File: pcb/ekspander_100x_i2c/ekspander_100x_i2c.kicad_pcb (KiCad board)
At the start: 4 copper layers, 500 x 100 mm, 156 parts, among them IC1 ESP32-S3-WROOM-1U-N16R8, J1 DG127A-5.08-06P-14-00AH, J10 DG127A-5.08-06P-14-00AH, J11 DG127A-5.08-06P-14-00AH, J12 DG127A-5.08-06P-14-00AH, J13 DG127A-5.08-06P-14-00AH, J14 DG127A-5.08-06P-14-00AH, J15 DG127A-5.08-06P-14-00AH, J16 DG127A-5.08-06P-14-00AH, J17 DG127A-5.08-06P-14-00AH, J18 DG127A-5.08-06P-14-00AH, J19 DG127A-5.08-06P-14-00AH, J2 DG127A-5.08-06P-14-00AH, J20 DG127A-5.08-06P-14-00AH, J21 DG127A-5.08-06P-14-00AH, J22 DG127A-5.08-06P-14-00AH, J23 DG127A-5.08-06P-14-00AH, J3 DG127A-5.08-06P-14-00AH, J4 DG127A-5.08-06P-14-00AH, J5 DG127A-5.08-06P-14-00AH, J6 DG127A-5.08-06P-14-00AH, J7 DG127A-5.08-06P-14-00AH, J8 DG127A-5.08-06P-14-00AH, J9 DG127A-5.08-06P-14-00AH, K1 G5Q-1A, K10 G5Q-1A, K11 G5Q-1A, K12 G5Q-1A, K13 G5Q-1A, K14 G5Q-1A, K15 G5Q-1A, K16 G5Q-1A, K17 G5Q-1A, K18 G5Q-1A, K19 G5Q-1A, K2 G5Q-1A, K20 G5Q-1A, K21 G5Q-1A, K22 G5Q-1A, K23 G5Q-1A, K24 G5Q-1A, K25 G5Q-1A, K26 G5Q-1A, K27 G5Q-1A, K28 G5Q-1A, K29 G5Q-1A, K3 G5Q-1A, K30 G5Q-1A, K31 G5Q-1A, K32 G5Q-1A, K33 G5Q-1A, K34 G5Q-1A, K35 G5Q-1A, K36 G5Q-1A, K37 G5Q-1A, K38 G5Q-1A, K39 G5Q-1A, K4 G5Q-1A, K40 G5Q-1A, K41 G5Q-1A, K42 G5Q-1A, K43 G5Q-1A, K44 G5Q-1A, K45 G5Q-1A, K46 G5Q-1A, K47 G5Q-1A, K48 G5Q-1A, K49 G5Q-1A, K5 G5Q-1A, K50 G5Q-1A, K6 G5Q-1A, K7 G5Q-1A, K8 G5Q-1A, K9 G5Q-1A, U1 MCP23017_SP, U10 ITS716G, U11 LTV-847, U12 ITS716G, U13 AP63203WU, U14 LTV-847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

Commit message: Ekspander 100x - finish J
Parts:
- removed C30: 0.1uF, Capacitor_SMD:C_0805_2012Metric_Pad1.18x1.45mm_HandSolder
- removed U39: ITS716G, Package_SO:SOIC-20W_7.5x12.8mm_P1.27mm
- removed U41: LTV-847, Package_DIP:DIP-16_W7.62mm
- moved U29 26.9 mm to (329.7, 58.3)
- moved U33 12.2 mm to (387.2, 59.2)
- moved U20 8.79 mm to (187.5, 56.8)
- moved U34 6.43 mm to (402.6, 59.2)
- moved U26 5.93 mm to (290.8, 57.8)
- moved U37 5.71 mm to (446.8, 60.1)
- moved U8 4.86 mm to (485.4, 56.8)
- moved U3 3.58 mm to (157.4, 57.3)
- moved U25 3.39 mm to (224.9, 56.6)
- moved U17 2.74 mm to (107.9, 57.3)
- moved U6 2.72 mm to (373.2, 58.1)
- moved U18 2.30 mm to (132.0, 55.5)
- moved U5 1.88 mm to (315.6, 57.6)
- moved U19 1.14 mm to (169.5, 58.6)
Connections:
- J10 pad 4: /U3 - U4/ZC69_OPEN_LED -> /U3 - U4/ZC70_CLOSE_LED
- J10 pad 5: /U3 - U4/ZC70_CLOSE_LED -> /U3 - U4/ZC69_OPEN_LED
- J11 pad 1: /U3 - U4/ZC72_OPEN_LED -> /U3 - U4/ZC71_OPEN_LED
- J11 pad 3: /U3 - U4/ZC71_OPEN_LED -> /U3 - U4/ZC72_OPEN_LED
- J14 pad 3: ZC76_OPEN_LED -> ZC75_OPEN_LED
- J14 pad 4: ZC76_CLOSE_LED -> ZC75_CLOSE_LED
- J14 pad 5: ZC75_CLOSE_LED -> ZC76_CLOSE_LED
- J14 pad 6: ZC75_OPEN_LED -> ZC76_OPEN_LED
- J17 pad 5: ZC80_OPEN_LED -> ZC80_CLOSE_LED
- J17 pad 6: ZC80_CLOSE_LED -> ZC80_OPEN_LED
- J6 pad 3: /U2/ZC63_CLOSE_LED -> /U2/ZC64_OPEN_LED
- J6 pad 4: /U2/ZC63_OPEN_LED -> /U2/ZC64_CLOSE_LED
- J6 pad 5: /U2/ZC64_CLOSE_LED -> /U2/ZC63_OPEN_LED
- J6 pad 6: /U2/ZC64_OPEN_LED -> /U2/ZC63_CLOSE_LED
- U17 pad 1: /U2/ZC63_CLOSE_LED -> /U2/ZC64_OPEN_LED
- U17 pad 3: /U2/ZC63_OPEN_LED -> /U2/ZC64_CLOSE_LED
- U17 pad 5: /U2/ZC64_CLOSE_LED -> /U2/ZC63_OPEN_LED
- U17 pad 7: /U2/ZC64_OPEN_LED -> /U2/ZC63_CLOSE_LED
- U19 pad 1: /U3 - U4/ZC67_CLOSE_LED -> /U3 - U4/ZC68_OPEN_LED
- U19 pad 3: /U3 - U4/ZC67_OPEN_LED -> /U3 - U4/ZC68_CLOSE_LED
- U19 pad 5: /U3 - U4/ZC68_CLOSE_LED -> /U3 - U4/ZC67_OPEN_LED
- U19 pad 7: /U3 - U4/ZC68_OPEN_LED -> /U3 - U4/ZC67_CLOSE_LED
- U2 pad 25: /U2/U2-GPA4 -> /U2/U2-GPA7
- U2 pad 26: /U2/U2-GPA5 -> /U2/U2-GPA6
- U2 pad 27: /U2/U2-GPA6 -> /U2/U2-GPA5
- U2 pad 28: /U2/U2-GPA7 -> /U2/U2-GPA4
- U3 pad 25: /U3 - U4/U3-GPA4 -> /U3 - U4/U3-GPA7
- U3 pad 26: /U3 - U4/U3-GPA5 -> /U3 - U4/U3-GPA6
- U3 pad 27: /U3 - U4/U3-GPA6 -> /U3 - U4/U3-GPA5
- U3 pad 28: /U3 - U4/U3-GPA7 -> /U3 - U4/U3-GPA4
- U30 pad 1: ZC77_OPEN_LED -> ZC78_OPEN_LED
- U30 pad 3: ZC77_CLOSE_LED -> ZC78_CLOSE_LED
- U30 pad 5: ZC78_CLOSE_LED -> ZC77_CLOSE_LED
- U30 pad 7: ZC78_OPEN_LED -> ZC77_OPEN_LED
- U33 pad 1: ZC79_OPEN_LED -> ZC80_CLOSE_LED
- U33 pad 3: ZC79_CLOSE_LED -> ZC80_OPEN_LED
- U33 pad 5: ZC80_CLOSE_LED -> ZC79_OPEN_LED
- U33 pad 7: ZC80_OPEN_LED -> ZC79_CLOSE_LED
- U37 pad 1: ZCX02_OPEN_LED -> ZCX03_OPEN_LED
- U37 pad 3: ZCX02_CLOSE_LED -> ZCX03_CLOSE_LED
- U37 pad 5: ZCX03_CLOSE_LED -> ZCX02_CLOSE_LED
- U37 pad 7: ZCX03_OPEN_LED -> ZCX02_OPEN_LED
- U4 pad 21: /U3 - U4/U4-GPA0 -> /U3 - U4/U4-GPA3
- U4 pad 22: /U3 - U4/U4-GPA1 -> /U3 - U4/U4-GPA2
- U4 pad 23: /U3 - U4/U4-GPA2 -> /U3 - U4/U4-GPA1
- U4 pad 24: /U3 - U4/U4-GPA3 -> /U3 - U4/U4-GPA0
- U5 pad 5: /U5/U5-GPB4 -> /U5/U5-GPB7
- U5 pad 6: /U5/U5-GPB5 -> /U5/U5-GPB6
- U5 pad 7: /U5/U5-GPB6 -> /U5/U5-GPB5
- U5 pad 8: /U5/U5-GPB7 -> /U5/U5-GPB4
- U6 pad 5: /U6/U6-GPB4 -> U6-GPB7
- U6 pad 6: /U6/U6-GPB5 -> U6-GPB6
- U6 pad 7: U6-GPB6 -> /U6/U6-GPB5
- U6 pad 8: U6-GPB7 -> /U6/U6-GPB4
- U7 pad 5: U7-GPB4 -> U7-GPB7
- U7 pad 6: U7-GPB5 -> U7-GPB6
- U7 pad 7: U7-GPB6 -> U7-GPB5
- U7 pad 8: U7-GPB7 -> U7-GPB4
- U8 pad 5: /U7 - U8/U8-GPB4 -> /U7 - U8/U8-GPB7
- U8 pad 6: /U7 - U8/U8-GPB5 -> /U7 - U8/U8-GPB6
- U8 pad 7: /U7 - U8/U8-GPB6 -> /U7 - U8/U8-GPB5
- U8 pad 8: /U7 - U8/U8-GPB7 -> /U7 - U8/U8-GPB4
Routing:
- net ZC74_OPEN_LED: track 0.00 -> 93.2 mm
- net ZC74_CLOSE_LED: track 0.00 -> 77.7 mm
- net ZCX02_OPEN_LED: track 0.00 -> 64.5 mm, vias 0 -> 1
- net /U2/ZC63_CLOSE_LED: track 0.00 -> 64.5 mm, vias 0 -> 1
- net ZC76_OPEN_LED: track 0.00 -> 60.6 mm, vias 0 -> 1
- net ZC77_OPEN_LED: track 0.00 -> 59.3 mm
- net ZC79_OPEN_LED: track 0.00 -> 58.3 mm, vias 0 -> 1
- net /U3 - U4/ZC70_OPEN_LED: track 0.00 -> 57.0 mm
- net /U3 - U4/ZC67_OPEN_LED: track 0.00 -> 56.5 mm, vias 0 -> 1
- net ZCX01_CLOSE_LED: track 0.00 -> 53.6 mm
- net /U3 - U4/ZC70_CLOSE_LED: track 0.00 -> 53.6 mm
- net ZCX03_CLOSE_LED: track 0.00 -> 52.2 mm, vias 0 -> 1
- net /U3 - U4/ZC67_CLOSE_LED: track 0.00 -> 52.2 mm, vias 0 -> 1
- net /U2/ZC64_CLOSE_LED: track 0.00 -> 52.1 mm, vias 0 -> 1
- net ZC79_CLOSE_LED: track 0.00 -> 52.1 mm, vias 0 -> 1
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
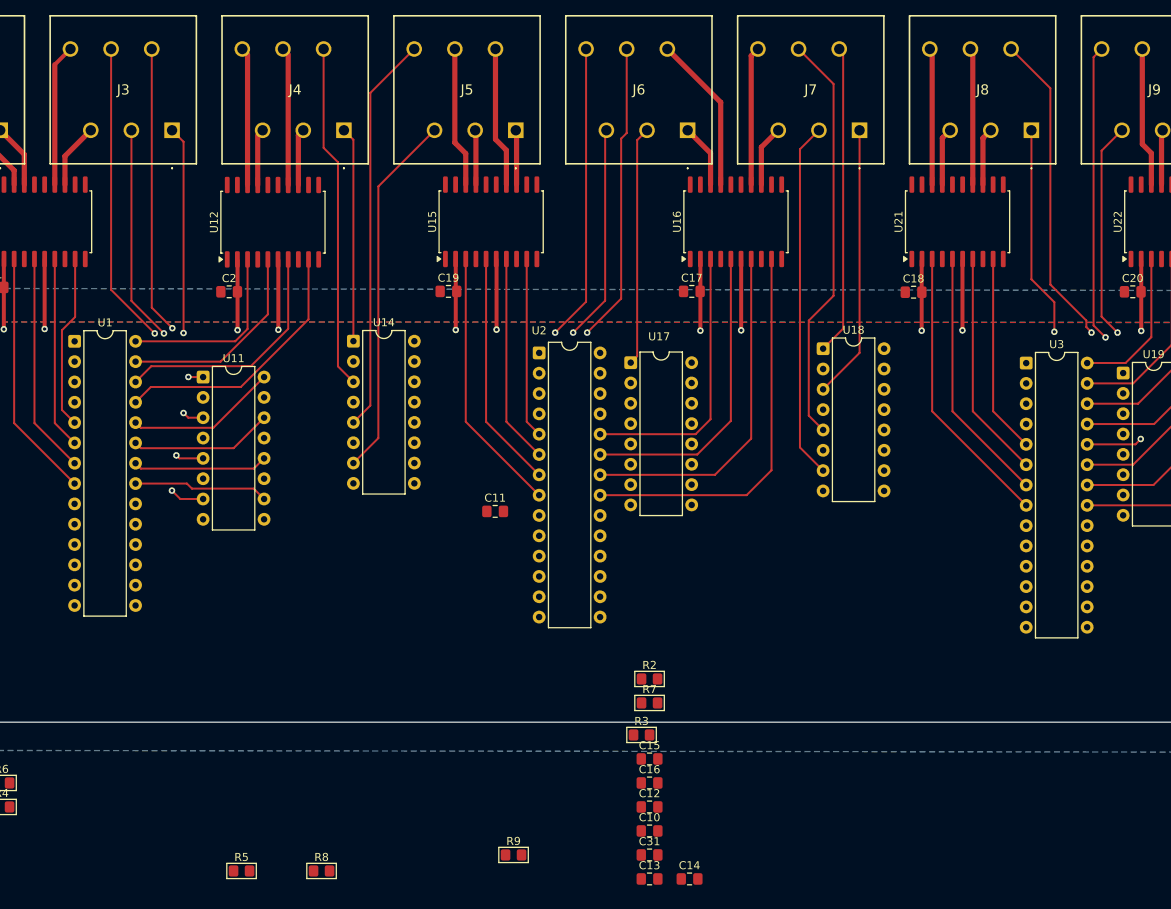
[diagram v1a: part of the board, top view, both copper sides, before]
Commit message: Remove temporary and backup files, update component properties in the I2C ekspander PCB design, and enhance the CSV with additional component details.
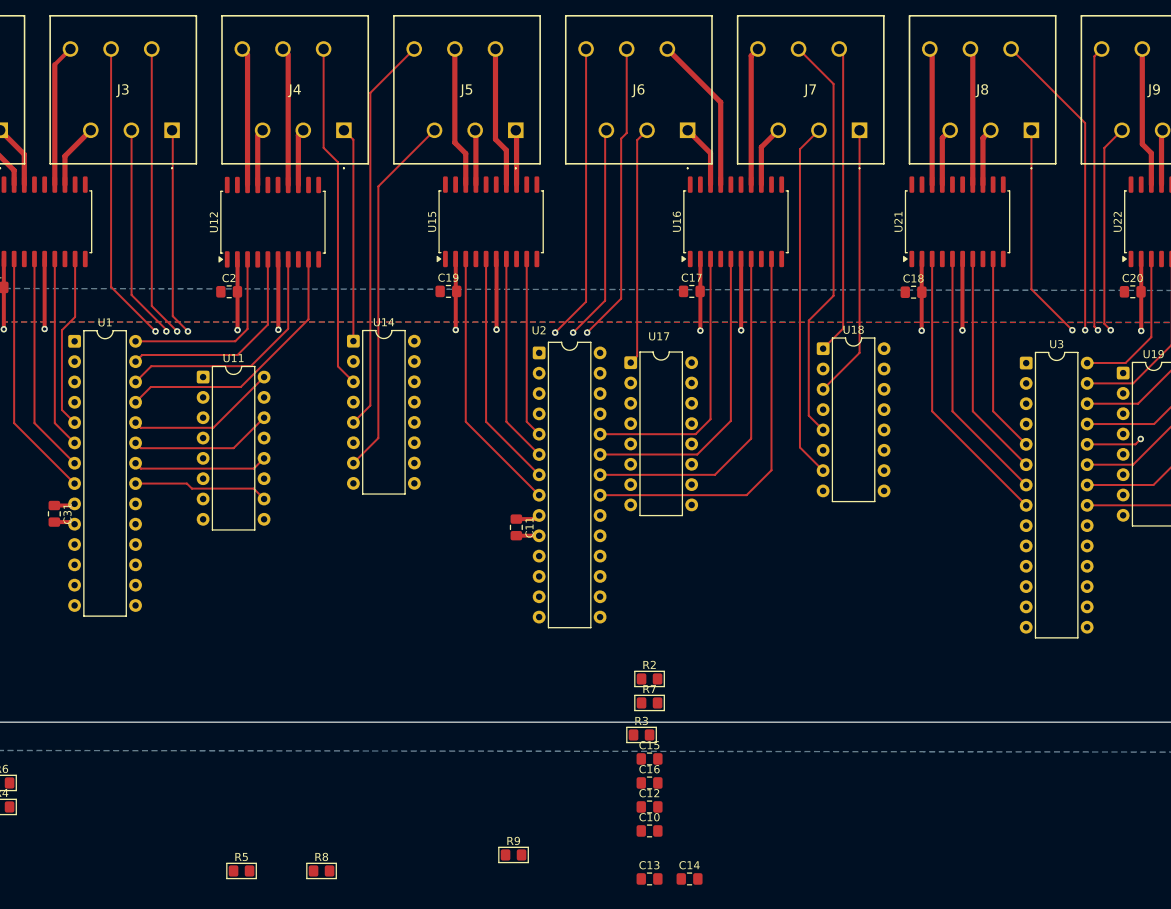
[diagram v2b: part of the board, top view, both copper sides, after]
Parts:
- moved C31 85.8 mm to (35.9, 76.2), turned to -90 degrees
- moved C11 3.32 mm to (93.7, 77.8), turned to -90 degrees
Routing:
- net +3V3: track 52.5 -> 58.2 mm
- net GND: track 353.0 -> 358.5 mm
- net /ZC60_CLOSE_LED: track 34.1 -> 32.5 mm, vias 2 -> 1
- net /ZC59_CLOSE_LED: track 46.5 -> 45.0 mm, vias 2 -> 1
- net /ZC59_OPEN_LED: track 62.7 -> 61.2 mm, vias 2 -> 1
- net /U3 - U4/ZC67_CLOSE_LED: track 52.2 -> 50.7 mm
- net /ZC60_OPEN_LED: track 49.8 -> 48.8 mm, vias 2 -> 1
- net /U1-GPA6: track 25.9 -> 26.6 mm
- added copper zone on In2.Cu, net +3V3

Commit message: Tech Explorations
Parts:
- moved R9 404.6 mm to (496.1, 81.2), turned to 90 degrees
- moved R8 374.6 mm to (441.9, 81.6), turned to 90 degrees
- moved C16 373.9 mm to (482.9, 78.3), turned to -90 degrees
- moved C15 319.8 mm to (428.9, 78.8), turned to -90 degrees
- moved R6 298.0 mm to (326.0, 82.0), turned to 90 degrees
- moved R7 274.4 mm to (384.1, 82.5), turned to 90 degrees
- moved C14 258.7 mm to (370.6, 79.8), turned to -90 degrees
- moved C13 207.2 mm to (313.1, 79.2), turned to -90 degrees
- moved R5 168.2 mm to (222.3, 79.7), turned to 90 degrees
- moved R4 142.0 mm to (167.8, 81.7), turned to 90 degrees
- moved C12 105.6 mm to (209.7, 77.0), turned to -90 degrees
- moved R2 63.9 mm to (48.9, 79.0), turned to 90 degrees
- moved C11 61.0 mm to (154.7, 79.0)
- moved C10 41.5 mm to (93.6, 77.8), turned to -90 degrees
- moved C8 38.2 mm to (261.6, 99.1)
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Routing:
- net SCK: track 0.00 -> 463.7 mm, vias 0 -> 2
- net SDA: track 0.00 -> 463.5 mm, vias 0 -> 2
- net RESET_U1: track 0.00 -> 202.0 mm
- net RESET_U2: track 0.00 -> 149.1 mm, vias 0 -> 1
- net RESET_U3: track 0.00 -> 91.0 mm, vias 0 -> 1
- net +3V3: track 58.2 -> 148.2 mm, vias 0 -> 8
- net +24V: track 95.0 -> 151.9 mm
- net RESET_U4: track 0.00 -> 38.0 mm, vias 0 -> 1
- net GND: track 358.5 -> 380.3 mm, vias 70 -> 91
- net RESET_U6: track 0.00 -> 3.34 mm
- net RESET_U8: track 0.00 -> 3.06 mm
- net RESET_U5: track 0.00 -> 2.79 mm
- net RESET_U7: track 0.00 -> 2.70 mm
- net ZC74_OPEN_LED: track 93.2 -> 94.9 mm, vias 0 -> 1
- net ZC74_CLOSE_LED: vias 0 -> 1
- added copper zone on F.Cu, net +3V3
